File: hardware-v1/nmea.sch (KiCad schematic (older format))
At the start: 24 parts, among them P1 CONN_01X20, U10 MCP2562, U11 SN65C1168E, U12 INA219

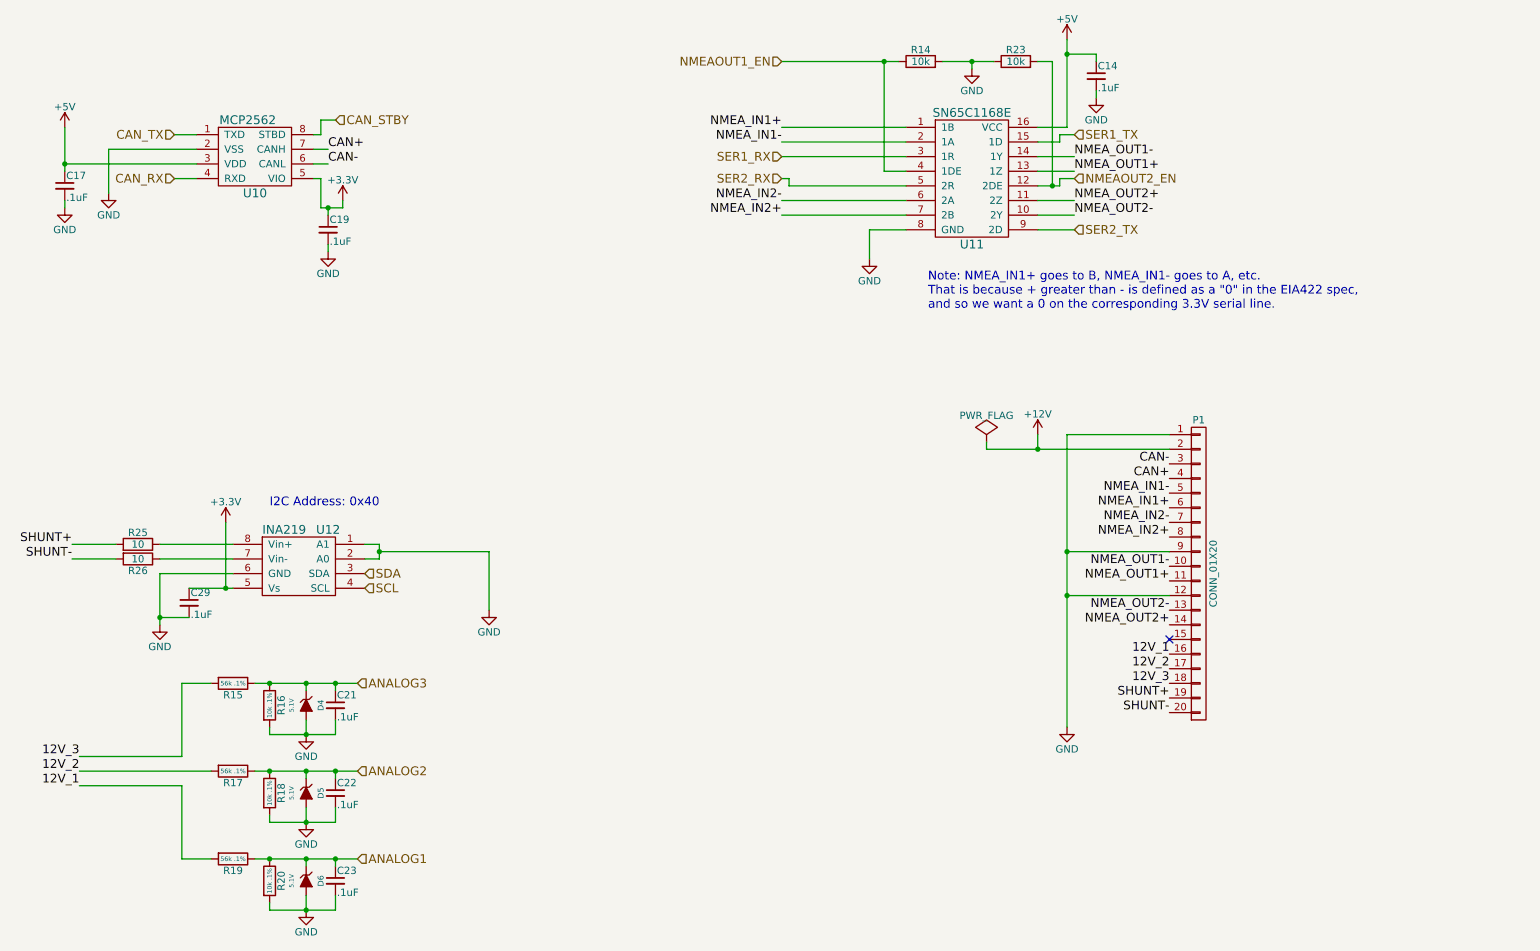
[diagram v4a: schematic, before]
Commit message: First draft of revision B
Lots of changes to the board. Almost completely re-layed out.

Will do some verification now.
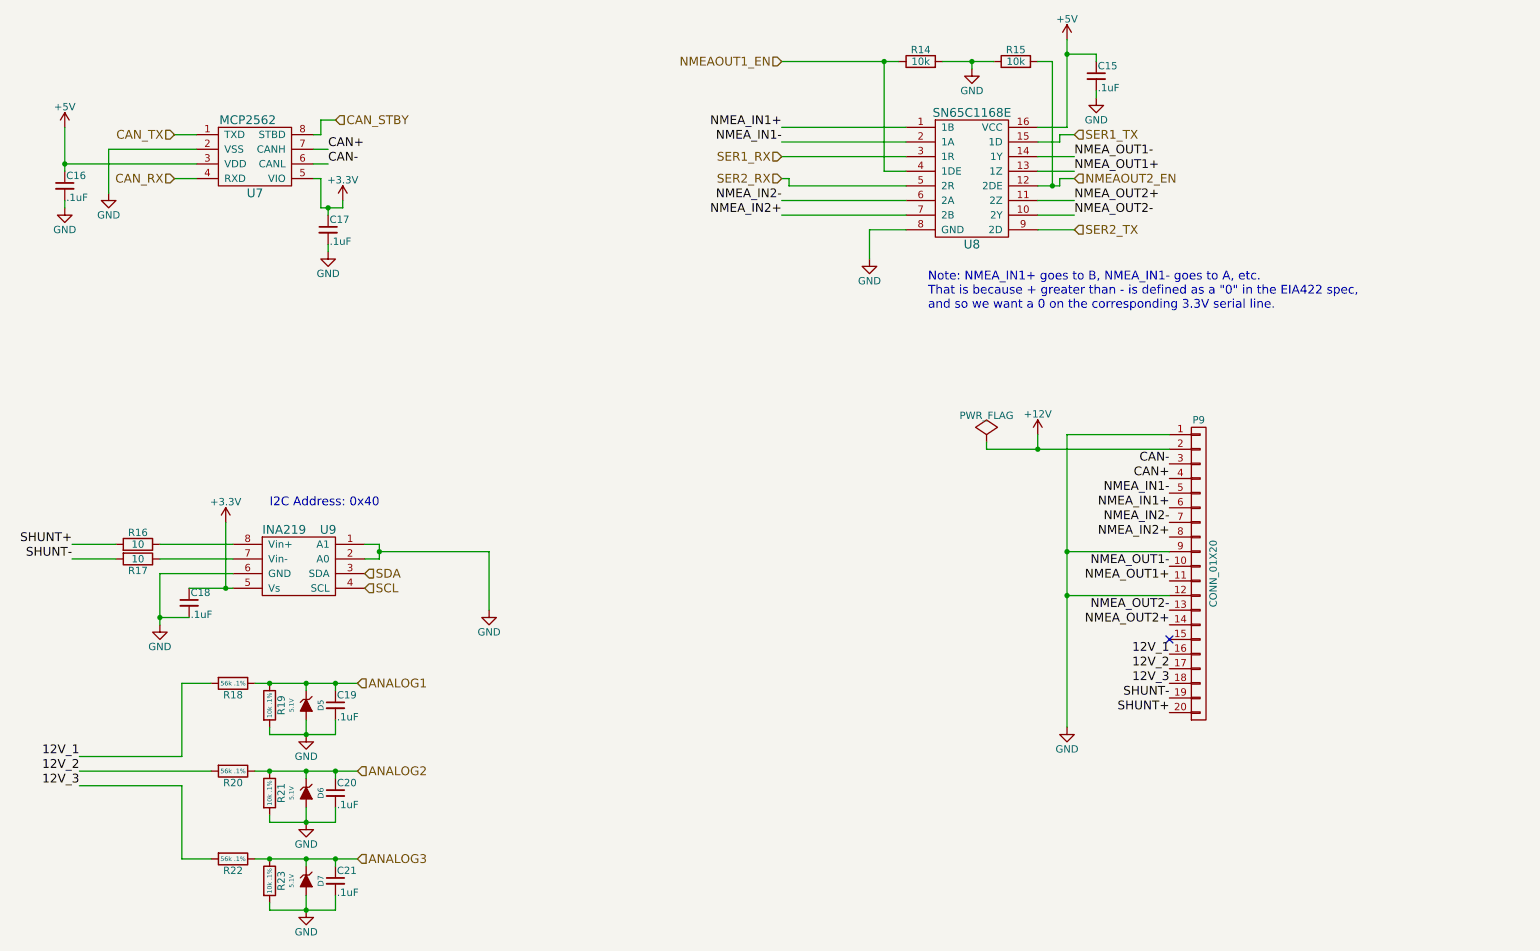
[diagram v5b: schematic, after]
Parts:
- R14: footprint Resistors_SMD:R_0603_HandSoldering -> Resistors_SMD:R_0603
- R15: renamed from R23; footprint Resistors_SMD:R_0603_HandSoldering -> Resistors_SMD:R_0603
- R18: renamed from R15; footprint Resistors_SMD:R_0603_HandSoldering -> Resistors_SMD:R_0603
- R19: renamed from R16; footprint Resistors_SMD:R_0603_HandSoldering -> Resistors_SMD:R_0603
- R20: renamed from R17; footprint Resistors_SMD:R_0603_HandSoldering -> Resistors_SMD:R_0603
- R21: renamed from R18; footprint Resistors_SMD:R_0603_HandSoldering -> Resistors_SMD:R_0603
- R22: renamed from R19; footprint Resistors_SMD:R_0603_HandSoldering -> Resistors_SMD:R_0603
- R23: renamed from R20; footprint Resistors_SMD:R_0603_HandSoldering -> Resistors_SMD:R_0603
- renumbered C14 to C15, C17 to C16, C19 to C17, C29 to C18, C21 to C19, C22 to C20, C23 to C21, D4 to D5, D5 to D6, D6 to D7, P1 to P9, R25 to R16, R26 to R17, U10 to U7, U11 to U8, U12 to U9
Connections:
- net 12V_1: now also R18.2; no longer R22.2
- net 12V_3: now also R22.2; no longer R18.2
- net ANALOG1: now also C19.1, D5.1 (K), R18.1, R19.1; no longer C21.1, D7.1 (K), R22.1, R23.1
- net ANALOG3: now also C21.1, D7.1 (K), R22.1, R23.1; no longer C19.1, D5.1 (K), R18.1, R19.1
- net SHUNT+: now also P9.20 (P20); no longer P9.19 (P19)
- net SHUNT-: now also P9.19 (P19); no longer P9.20 (P20)

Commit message: Finalizing revB
 - Added part numbers on all parts (in kicad PartNumber field)
 - Some finicking in a bunch of corners
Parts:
- C15, C16, C17, C18, C19, C20, C21: PartNumber (none) -> CC0603KPX7R7BB104
- D5, D6, D7: PartNumber (none) -> MM3Z5V1ST1G
- P9: PartNumber (none) -> 1709678
- R14, R15: PartNumber (none) -> RC0603JR-0710KL
- R16, R17: PartNumber (none) -> RC0603FR-0710RL
- R18, R20, R22: PartNumber (none) -> ERA-3AEB563V
- R19, R21, R23: PartNumber (none) -> AT0603BRD0710KL
- U7: PartNumber (none) -> MCP2562T-E/SN
- U8: PartNumber (none) -> SN65C1168EPWR
- U9: PartNumber (none) -> INA219BIDR
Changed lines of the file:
@@
 F 2 "Resistors_SMD:R_0603" V 2680 5500 30  0001 C CNN
 F 3 "" H 2750 5500 30  0000 C CNN
+F 4 "ERA-3AEB563V" V 2750 5500 60  0001 C CNN "PartNumber"
 	1    2750 5500
 	0    1    1    0
@@
 F 2 "Resistors_SMD:R_0603" V 2930 5650 30  0001 C CNN
 F 3 "" H 3000 5650 30  0000 C CNN
+F 4 "AT0603BRD0710KL" V 3000 5650 60  0001 C CNN "PartNumber"
 	1    3000 5650
 	1    0    0    -1
@@
 F 2 "Diodes_SMD:SOD-323" H 3250 5650 60  0001 C CNN
 F 3 "" H 3250 5650 60  0000 C CNN
+F 4 "MM3Z5V1ST1G" H 3250 5650 60  0001 C CNN "PartNumber"
 	1    3250 5650
 	0    1    1    0
@@
 F 2 "Capacitors_SMD:C_0603" H 3450 5650 60  0001 C CNN
 F 3 "" H 3450 5650 60  0000 C CNN
+F 4 "CC0603KPX7R7BB104" H 3450 5650 60  0001 C CNN "PartNumber"
 	1    3450 5650
 	1    0    0    -1
@@
 F 2 "bb:SOIC8N" H 2900 1750 60  0001 C CNN
 F 3 "" H 2900 1750 60  0000 C CNN
+F 4 "MCP2562T-E/SN" H 2900 1850 60  0001 C CNN "PartNumber"
 	1    2900 1850
 	1    0    0    -1
@@
 F 2 "Capacitors_SMD:C_0603" H 3400 2400 60  0001 C CNN
 F 3 "" H 3400 2400 60  0000 C CNN
+F 4 "CC0603KPX7R7BB104" H 3400 2400 60  0001 C CNN "PartNumber"
 	1    3400 2400
 	1    0    0    -1
@@
 F 2 "Capacitors_SMD:C_0603" H 1600 2100 60  0001 C CNN
 F 3 "" H 1600 2100 60  0000 C CNN
+F 4 "CC0603KPX7R7BB104" H 1600 2100 60  0001 C CNN "PartNumber"
 	1    1600 2100
 	1    0    0    -1
@@
 F 2 "Resistors_SMD:R_0603" V 2680 6100 30  0001 C CNN
 F 3 "" H 2750 6100 30  0000 C CNN
+F 4 "ERA-3AEB563V" V 2750 6100 60  0001 C CNN "PartNumber"
 	1    2750 6100
 	0    1    1    0
@@
 F 2 "Resistors_SMD:R_0603" V 2930 6250 30  0001 C CNN
 F 3 "" H 3000 6250 30  0000 C CNN
+F 4 "AT0603BRD0710KL" V 3000 6250 60  0001 C CNN "PartNumber"
 	1    3000 6250
 	1    0    0    -1
@@
 F 2 "Diodes_SMD:SOD-323" H 3250 6250 60  0001 C CNN
 F 3 "" H 3250 6250 60  0000 C CNN
+F 4 "MM3Z5V1ST1G" H 3250 6250 60  0001 C CNN "PartNumber"
 	1    3250 6250
 	0    1    1    0
@@
 F 2 "Capacitors_SMD:C_0603" H 3450 6250 60  0001 C CNN
 F 3 "" H 3450 6250 60  0000 C CNN
+F 4 "CC0603KPX7R7BB104" H 3450 6250 60  0001 C CNN "PartNumber"
 	1    3450 6250
 	1    0    0    -1
@@
 F 2 "Resistors_SMD:R_0603" V 2680 6700 30  0001 C CNN
 F 3 "" H 2750 6700 30  0000 C CNN
+F 4 "ERA-3AEB563V" V 2750 6700 60  0001 C CNN "PartNumber"
 	1    2750 6700
 	0    1    1    0
@@
 F 2 "Resistors_SMD:R_0603" V 2930 6850 30  0001 C CNN
 F 3 "" H 3000 6850 30  0000 C CNN
+F 4 "AT0603BRD0710KL" V 3000 6850 60  0001 C CNN "PartNumber"
 	1    3000 6850
 	1    0    0    -1
@@
 F 2 "Diodes_SMD:SOD-323" H 3250 6850 60  0001 C CNN
 F 3 "" H 3250 6850 60  0000 C CNN
+F 4 "MM3Z5V1ST1G" H 3250 6850 60  0001 C CNN "PartNumber"
 	1    3250 6850
 	0    1    1    0
@@
 F 2 "Capacitors_SMD:C_0603" H 3450 6850 60  0001 C CNN
 F 3 "" H 3450 6850 60  0000 C CNN
+F 4 "CC0603KPX7R7BB104" H 3450 6850 60  0001 C CNN "PartNumber"
 	1    3450 6850
 	1    0    0    -1
@@
 F 2 "bb:SOIC8N" H 3200 4700 60  0001 C CNN
 F 3 "" H 3200 4700 60  0000 C CNN
+F 4 "INA219BIDR" H 3200 4700 60  0001 C CNN "PartNumber"
 	1    3200 4700
 	1    0    0    -1
@@
 F 2 "Capacitors_SMD:C_0603" H 2450 4950 60  0001 C CNN
 F 3 "" H 2450 4950 60  0000 C CNN
+F 4 "CC0603KPX7R7BB104" H 2450 4950 60  0001 C CNN "PartNumber"
 	1    2450 4950
 	1    0    0    -1
@@
 F 2 "Housings_SSOP:TSSOP-16_4.4x5mm_Pitch0.65mm" H 7800 2150 60  0001 C CNN
 F 3 "" H 7800 2150 60  0000 C CNN
+F 4 "SN65C1168EPWR" H 7800 2150 60  0001 C CNN "PartNumber"
 	1    7800 2150
 	1    0    0    -1
@@
 F 2 "Capacitors_SMD:C_0603" H 8650 1350 60  0001 C CNN
 F 3 "" H 8650 1350 60  0000 C CNN
+F 4 "CC0603KPX7R7BB104" H 8650 1350 60  0001 C CNN "PartNumber"
 	1    8650 1350
 	1    0    0    -1
@@
 F 2 "Resistors_SMD:R_0603" V 7380 1250 30  0001 C CNN
 F 3 "" H 7450 1250 30  0000 C CNN
+F 4 "RC0603JR-0710KL" H 7450 1250 60  0001 C CNN "PartNumber"
 	1    7450 1250
 	0    -1   -1   0
@@
 F 2 "Resistors_SMD:R_0603" V 8030 1250 30  0001 C CNN
 F 3 "" H 8100 1250 30  0000 C CNN
+F 4 "RC0603JR-0710KL" H 8100 1250 60  0001 C CNN "PartNumber"
 	1    8100 1250
 	0    -1   -1   0
@@
 F 2 "bb:TerminalBlock_Pheonix_PT-3.5mm_20pol" H 9350 4750 60  0001 C CNN
 F 3 "" H 9350 4750 60  0000 C CNN
+F 4 "1709678" H 9350 4750 60  0001 C CNN "PartNumber"
 	1    9350 4750
 	1    0    0    -1
@@
 F 2 "Resistors_SMD:R_0603" V 2030 4550 50  0001 C CNN
 F 3 "" H 2100 4550 50  0000 C CNN
+F 4 "RC0603FR-0710RL" H 2100 4550 60  0001 C CNN "PartNumber"
 	1    2100 4550
 	0    1    -1   0
@@
 F 2 "Resistors_SMD:R_0603" V 2030 4650 50  0001 C CNN
 F 3 "" H 2100 4650 50  0000 C CNN
+F 4 "RC0603FR-0710RL" H 2100 4650 60  0001 C CNN "PartNumber"
 	1    2100 4650
 	0    1    1    0

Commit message: Final touches + v1revb sent to oshpark
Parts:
- renumbered C15 to C14, C16 to C15, C17 to C16, C18 to C17, C19 to C18, C20 to C19, C21 to C20, D5 to D7, D6 to D8, D7 to D9, P9 to P7
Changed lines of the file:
@@
 $EndComp
 $Comp
-L ZENERsmall D5
+L ZENERsmall D7
 U 1 1 5660858A
 P 3250 5650
-F 0 "D5" H 3250 5750 40  0000 C CNN
+F 0 "D7" H 3250 5750 40  0000 C CNN
 F 1 "5.1V" H 3250 5550 30  0000 C CNN
 F 2 "Diodes_SMD:SOD-323" H 3250 5650 60  0001 C CNN
@@
 $EndComp
 $Comp
-L C_Small C19
+L C_Small C18
 U 1 1 56608592
 P 3450 5650
-F 0 "C19" H 3460 5720 50  0000 L CNN
+F 0 "C18" H 3460 5720 50  0000 L CNN
 F 1 ".1uF" H 3460 5570 50  0000 L CNN
 F 2 "Capacitors_SMD:C_0603" H 3450 5650 60  0001 C CNN
@@
 $EndComp
 $Comp
-L GND #PWR050
+L GND #PWR049
 U 1 1 5660859F
 P 3250 5850
-F 0 "#PWR050" H 3250 5600 50  0001 C CNN
+F 0 "#PWR049" H 3250 5600 50  0001 C CNN
 F 1 "GND" H 3250 5700 50  0000 C CNN
 F 2 "" H 3250 5850 60  0000 C CNN
@@
 $EndComp
 $Comp
-L +3.3V #PWR051
+L +3.3V #PWR050
 U 1 1 5661817C
 P 3500 2200
-F 0 "#PWR051" H 3500 2050 50  0001 C CNN
+F 0 "#PWR050" H 3500 2050 50  0001 C CNN
 F 1 "+3.3V" H 3500 2340 50  0000 C CNN
 F 2 "" H 3500 2200 60  0000 C CNN
@@
 $EndComp
 $Comp
-L GND #PWR052
+L GND #PWR051
 U 1 1 5661CF45
 P 1900 2150
-F 0 "#PWR052" H 1900 1900 50  0001 C CNN
+F 0 "#PWR051" H 1900 1900 50  0001 C CNN
 F 1 "GND" H 1900 2000 50  0000 C CNN
 F 2 "" H 1900 2150 60  0000 C CNN
@@
 $EndComp
 $Comp
-L +5V #PWR053
+L +5V #PWR052
 U 1 1 5661EB70
 P 1600 1700
-F 0 "#PWR053" H 1600 1550 50  0001 C CNN
+F 0 "#PWR052" H 1600 1550 50  0001 C CNN
 F 1 "+5V" H 1600 1840 50  0000 C CNN
 F 2 "" H 1600 1700 60  0000 C CNN
@@
 CAN_STBY
 $Comp
-L C_Small C17
+L C_Small C16
 U 1 1 566311B1
 P 3400 2400
-F 0 "C17" H 3410 2470 50  0000 L CNN
+F 0 "C16" H 3410 2470 50  0000 L CNN
 F 1 ".1uF" H 3410 2320 50  0000 L CNN
 F 2 "Capacitors_SMD:C_0603" H 3400 2400 60  0001 C CNN
@@
 $EndComp
 $Comp
-L GND #PWR054
+L GND #PWR053
 U 1 1 5663157A
 P 3400 2550
-F 0 "#PWR054" H 3400 2300 50  0001 C CNN
+F 0 "#PWR053" H 3400 2300 50  0001 C CNN
 F 1 "GND" H 3400 2400 50  0000 C CNN
 F 2 "" H 3400 2550 60  0000 C CNN
@@
 $EndComp
 $Comp
-L C_Small C16
+L C_Small C15
 U 1 1 566339F9
 P 1600 2100
-F 0 "C16" H 1610 2170 50  0000 L CNN
+F 0 "C15" H 1610 2170 50  0000 L CNN
 F 1 ".1uF" H 1610 2020 50  0000 L CNN
 F 2 "Capacitors_SMD:C_0603" H 1600 2100 60  0001 C CNN
@@
 $EndComp
 $Comp
-L GND #PWR055
+L GND #PWR054
 U 1 1 56633AB1
 P 1600 2250
-F 0 "#PWR055" H 1600 2000 50  0001 C CNN
+F 0 "#PWR054" H 1600 2000 50  0001 C CNN
 F 1 "GND" H 1600 2100 50  0000 C CNN
 F 2 "" H 1600 2250 60  0000 C CNN
@@
 $EndComp
 $Comp
-L ZENERsmall D6
+L ZENERsmall D8
 U 1 1 5671B30D
 P 3250 6250
-F 0 "D6" H 3250 6350 40  0000 C CNN
+F 0 "D8" H 3250 6350 40  0000 C CNN
 F 1 "5.1V" H 3250 6150 30  0000 C CNN
 F 2 "Diodes_SMD:SOD-323" H 3250 6250 60  0001 C CNN
@@
 $EndComp
 $Comp
-L C_Small C20
+L C_Small C19
 U 1 1 5671B314
 P 3450 6250
-F 0 "C20" H 3460 6320 50  0000 L CNN
+F 0 "C19" H 3460 6320 50  0000 L CNN
 F 1 ".1uF" H 3460 6170 50  0000 L CNN
 F 2 "Capacitors_SMD:C_0603" H 3450 6250 60  0001 C CNN
@@
 $EndComp
 $Comp
-L GND #PWR056
+L GND #PWR055
 U 1 1 5671B320
 P 3250 6450
-F 0 "#PWR056" H 3250 6200 50  0001 C CNN
+F 0 "#PWR055" H 3250 6200 50  0001 C CNN
 F 1 "GND" H 3250 6300 50  0000 C CNN
 F 2 "" H 3250 6450 60  0000 C CNN
@@
 $EndComp
 $Comp
-L ZENERsmall D7
+L ZENERsmall D9
 U 1 1 5671D28C
 P 3250 6850
-F 0 "D7" H 3250 6950 40  0000 C CNN
+F 0 "D9" H 3250 6950 40  0000 C CNN
 F 1 "5.1V" H 3250 6750 30  0000 C CNN
 F 2 "Diodes_SMD:SOD-323" H 3250 6850 60  0001 C CNN
@@
 $EndComp
 $Comp
-L C_Small C21
+L C_Small C20
 U 1 1 5671D293
 P 3450 6850
-F 0 "C21" H 3460 6920 50  0000 L CNN
+F 0 "C20" H 3460 6920 50  0000 L CNN
 F 1 ".1uF" H 3460 6770 50  0000 L CNN
 F 2 "Capacitors_SMD:C_0603" H 3450 6850 60  0001 C CNN
@@
 $EndComp
 $Comp
-L GND #PWR057
+L GND #PWR056
 U 1 1 5671D29F
 P 3250 7050
-F 0 "#PWR057" H 3250 6800 50  0001 C CNN
+F 0 "#PWR056" H 3250 6800 50  0001 C CNN
 F 1 "GND" H 3250 6900 50  0000 C CNN
 F 2 "" H 3250 7050 60  0000 C CNN
@@
 ANALOG3
 $Comp
-L +12V #PWR058
+L +12V #PWR057
 U 1 1 567F4FFA
 P 8250 3800
-F 0 "#PWR058" H 8250 3650 50  0001 C CNN
+F 0 "#PWR057" H 8250 3650 50  0001 C CNN
 F 1 "+12V" H 8250 3940 50  0000 C CNN
 F 2 "" H 8250 3800 60  0000 C CNN
@@
 $EndComp
 $Comp
-L GND #PWR059
+L GND #PWR058
 U 1 1 56805BCC
 P 2250 5100
-F 0 "#PWR059" H 2250 4850 50  0001 C CNN
+F 0 "#PWR058" H 2250 4850 50  0001 C CNN
 F 1 "GND" H 2250 4950 50  0000 C CNN
 F 2 "" H 2250 5100 60  0000 C CNN
@@
 $EndComp
 $Comp
-L PWR_FLAG #FLG060
+L PWR_FLAG #FLG059
 U 1 1 568074D6
 P 7900 3850
-F 0 "#FLG060" H 7900 3945 50  0001 C CNN
+F 0 "#FLG059" H 7900 3945 50  0001 C CNN
 F 1 "PWR_FLAG" H 7900 4030 50  0000 C CNN
 F 2 "" H 7900 3850 60  0000 C CNN
@@
 $EndComp
 $Comp
-L +3.3V #PWR061
+L +3.3V #PWR060
 U 1 1 56699F39
 P 2700 4400
-F 0 "#PWR061" H 2700 4250 50  0001 C CNN
+F 0 "#PWR060" H 2700 4250 50  0001 C CNN
 F 1 "+3.3V" H 2700 4540 50  0000 C CNN
 F 2 "" H 2700 4400 60  0000 C CNN
@@
 $EndComp
 $Comp
-L GND #PWR062
+L GND #PWR061
 U 1 1 5669B7A7
 P 4500 5000
-F 0 "#PWR062" H 4500 4750 50  0001 C CNN
+F 0 "#PWR061" H 4500 4750 50  0001 C CNN
 F 1 "GND" H 4500 4850 50  0000 C CNN
 F 2 "" H 4500 5000 60  0000 C CNN
@@
 SCL
 $Comp
-L C_Small C18
+L C_Small C17
 U 1 1 566A03FA
 P 2450 4950
-F 0 "C18" H 2460 5020 50  0000 L CNN
+F 0 "C17" H 2460 5020 50  0000 L CNN
 F 1 ".1uF" H 2460 4870 50  0000 L CNN
 F 2 "Capacitors_SMD:C_0603" H 2450 4950 60  0001 C CNN
@@
 $EndComp
 $Comp
-L +5V #PWR063
+L +5V #PWR062
 U 1 1 5665D00E
 P 8450 1100
-F 0 "#PWR063" H 8450 950 50  0001 C CNN
+F 0 "#PWR062" H 8450 950 50  0001 C CNN
 F 1 "+5V" H 8450 1240 50  0000 C CNN
 F 2 "" H 8450 1100 60  0000 C CNN
@@
 $EndComp
 $Comp
-L C_Small C15
+L C_Small C14
 U 1 1 5665D07C
 P 8650 1350
-F 0 "C15" H 8660 1420 50  0000 L CNN
+F 0 "C14" H 8660 1420 50  0000 L CNN
 F 1 ".1uF" H 8660 1270 50  0000 L CNN
 F 2 "Capacitors_SMD:C_0603" H 8650 1350 60  0001 C CNN
@@
 $EndComp
 $Comp
-L GND #PWR064
+L GND #PWR063
 U 1 1 5665D465
 P 8650 1500
-F 0 "#PWR064" H 8650 1250 50  0001 C CNN
+F 0 "#PWR063" H 8650 1250 50  0001 C CNN
 F 1 "GND" H 8650 1350 50  0000 C CNN
 F 2 "" H 8650 1500 60  0000 C CNN
@@
 $EndComp
 $Comp
-L GND #PWR065
+L GND #PWR064
 U 1 1 566617E0
 P 7100 2600
-F 0 "#PWR065" H 7100 2350 50  0001 C CNN
+F 0 "#PWR064" H 7100 2350 50  0001 C CNN
 F 1 "GND" H 7100 2450 50  0000 C CNN
 F 2 "" H 7100 2600 60  0000 C CNN
@@
 $EndComp
 $Comp
-L GND #PWR066
+L GND #PWR065
 U 1 1 5667B0C5
 P 7800 1300
-F 0 "#PWR066" H 7800 1050 50  0001 C CNN
+F 0 "#PWR065" H 7800 1050 50  0001 C CNN
 F 1 "GND" H 7800 1150 50  0000 C CNN
 F 2 "" H 7800 1300 60  0000 C CNN
@@
 Connection ~ 7800 1250
 $Comp
-L CONN_01X20 P9
+L CONN_01X20 P7
 U 1 1 566AE4E8
 P 9350 4750
-F 0 "P9" H 9350 5800 50  0000 C CNN
+F 0 "P7" H 9350 5800 50  0000 C CNN
 F 1 "CONN_01X20" V 9450 4750 50  0000 C CNN
 F 2 "bb:TerminalBlock_Pheonix_PT-3.5mm_20pol" H 9350 4750 60  0001 C CNN
@@
 Connection ~ 8450 4900
 $Comp
-L GND #PWR067
+L GND #PWR066
 U 1 1 566C9EC9
 P 8450 5800
-F 0 "#PWR067" H 8450 5550 50  0001 C CNN
+F 0 "#PWR066" H 8450 5550 50  0001 C CNN
 F 1 "GND" H 8450 5650 50  0000 C CNN
 F 2 "" H 8450 5800 60  0000 C CNN

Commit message: Change reference of 10k .1% resistors
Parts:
- R19, R21, R23: PartNumber AT0603BRD0710KL -> P10KDBCT-ND
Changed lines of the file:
@@
 F 2 "Resistors_SMD:R_0603" V 2930 5650 30  0001 C CNN
 F 3 "" H 3000 5650 30  0000 C CNN
-F 4 "AT0603BRD0710KL" V 3000 5650 60  0001 C CNN "PartNumber"
+F 4 "P10KDBCT-ND" V 3000 5650 60  0001 C CNN "PartNumber"
 	1    3000 5650
 	1    0    0    -1
@@
 F 2 "Resistors_SMD:R_0603" V 2930 6250 30  0001 C CNN
 F 3 "" H 3000 6250 30  0000 C CNN
-F 4 "AT0603BRD0710KL" V 3000 6250 60  0001 C CNN "PartNumber"
+F 4 "P10KDBCT-ND" V 3000 6250 60  0001 C CNN "PartNumber"
 	1    3000 6250
 	1    0    0    -1
@@
 F 2 "Resistors_SMD:R_0603" V 2930 6850 30  0001 C CNN
 F 3 "" H 3000 6850 30  0000 C CNN
-F 4 "AT0603BRD0710KL" V 3000 6850 60  0001 C CNN "PartNumber"
+F 4 "P10KDBCT-ND" V 3000 6850 60  0001 C CNN "PartNumber"
 	1    3000 6850
 	1    0    0    -1
